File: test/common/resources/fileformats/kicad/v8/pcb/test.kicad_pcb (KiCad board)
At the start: 2 copper layers, 4 parts

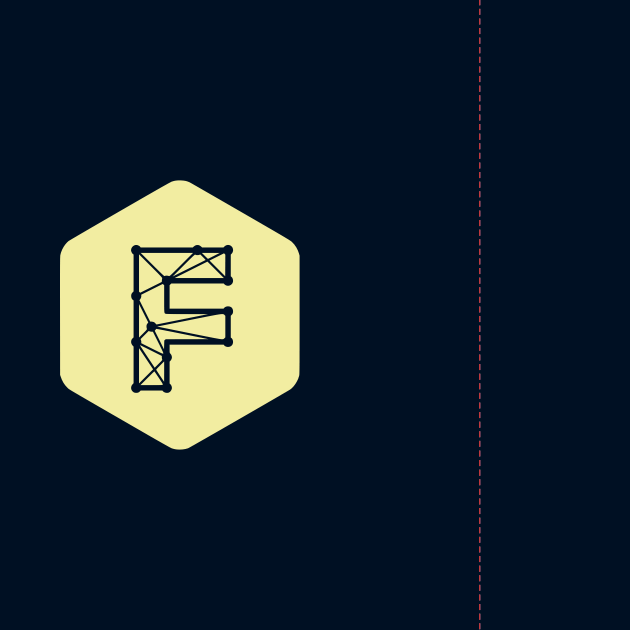
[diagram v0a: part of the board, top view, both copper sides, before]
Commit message: Restore Atopile Local 0.2 on pinned 0.15.9 sources
Import the publicly distributed atopile 0.15.9 PyPI source release as the
compiler/UI baseline, retaining upstream main as its historical parent.
PyPI source SHA256: 681cc1e123646dd133de31b631aedaf4eaac88682613b4f82d1da4b3ef8b4e8e.

Revive the local VS Code extension with a separate identity and launcher,
isolated state, bundled visualization assets, and provider settings. Bridge
the existing Atopile tool harness to a natively signed-in Codex app-server
for ChatGPT-plan use, retaining direct API providers as explicit options.
Include local part import, layout tools, packaging/runtime setup and tests.

Preserve upstream licensing, restored GitHub metadata and source notices.
Exclude local environments, generated webview bundles and personal QA paths.
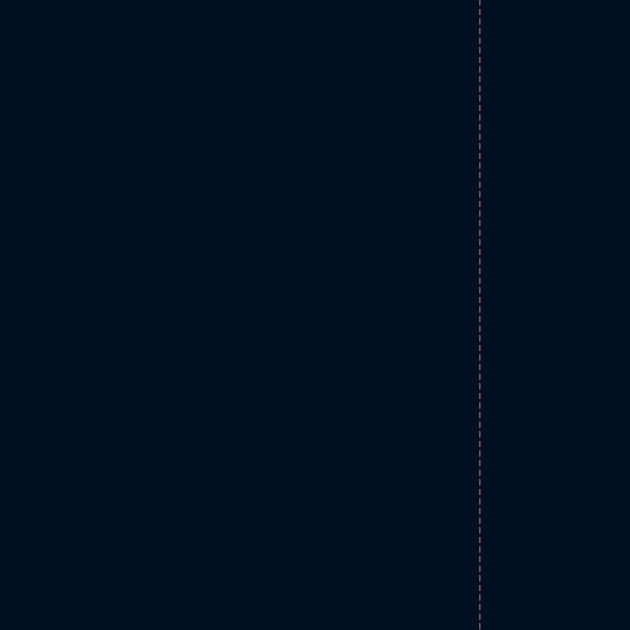
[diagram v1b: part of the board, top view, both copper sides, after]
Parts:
- G***: moved to B.Cu
- moved G*** 178.9 mm to (90.0, 180.0), turned to 180 degrees
